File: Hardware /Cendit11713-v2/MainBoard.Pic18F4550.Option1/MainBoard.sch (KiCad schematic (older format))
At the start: 54 parts, among them J1 RESET_CON

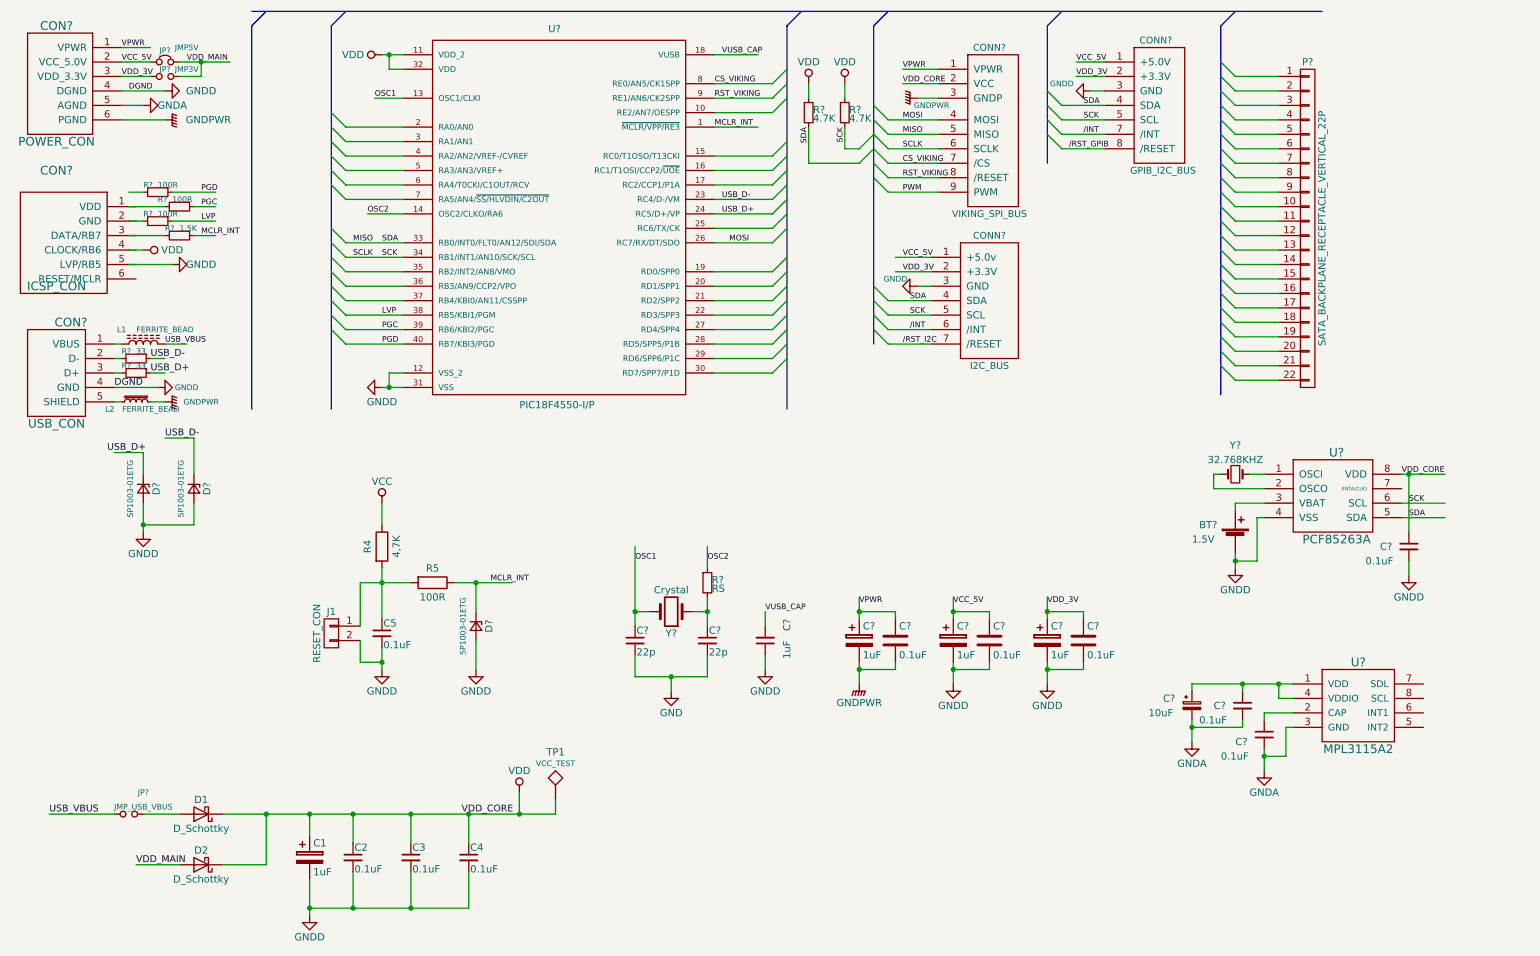
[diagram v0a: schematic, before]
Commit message: Trabajo en Cendit11713 + CenditLab.Reducido
  - En CenditLab revision de codigo
  - En Cendit11713 diseño de tarjeta madre, se crean dos opciones
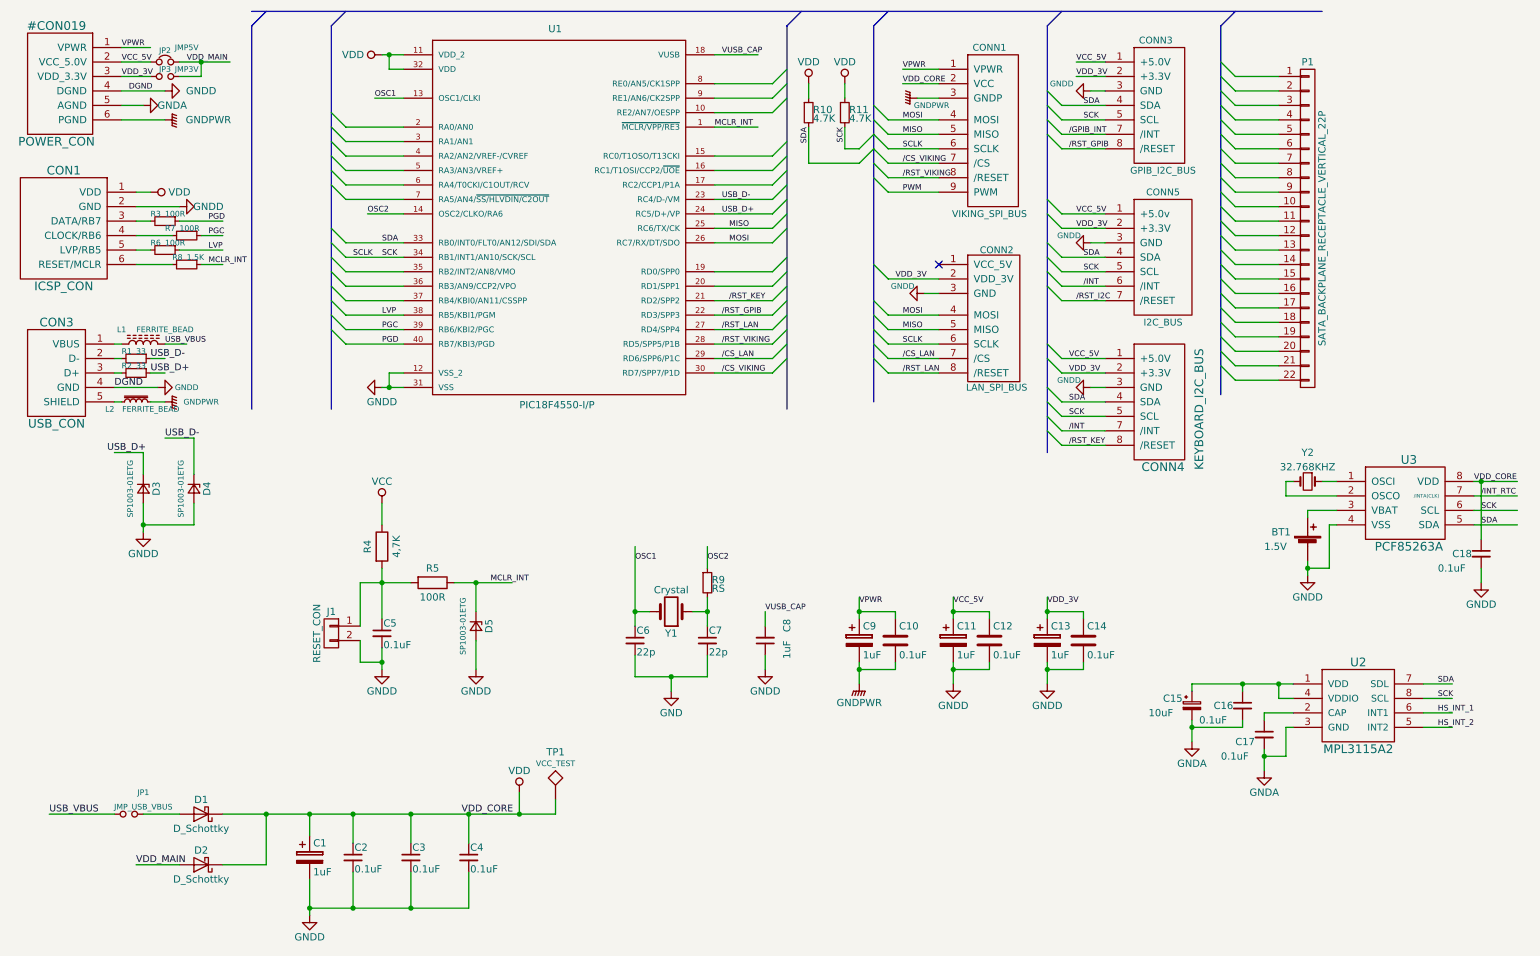
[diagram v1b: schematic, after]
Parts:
- removed CON?: ICSP_CON, symbol ICSP_CON
- removed CON?: POWER_CON, symbol POWER_CON
- added CON1: ICSP_CON, Pin_Headers:Pin_Header_Straight_2x03_Pitch2.54mm, symbol ICSP_CON
- added CONN2: LAN_SPI_BUS, CenditFootprints:SATA_RECEPTACLE_VERTICAL_SMT_6P_7P, symbol LAN_SPI_BUS
- added CONN4: KEYBOARD_I2C_BUS, CenditFootprints:SATA_RECEPTACLE_VERTICAL_SMT_6P_7P, symbol KEYBOARD_I2C_BUS
- C1: footprint (none) -> Capacitors_SMD:C_1206_HandSoldering
- C10, C12, C14, C16, C17, C18: renamed from C?; footprint (none) -> Capacitors_SMD:C_0805_HandSoldering
- C11, C13, C15, C8, C9: renamed from C?; footprint (none) -> Capacitors_SMD:C_1206_HandSoldering
- C2, C3, C4, C5: footprint (none) -> Capacitors_SMD:C_0805_HandSoldering
- C6, C7: renamed from C?; footprint (none) -> Capacitors_SMD:C_0603_HandSoldering
- CON3: renamed from CON?; footprint (none) -> CenditFootprints:USB_SMT_B
- CONN1, CONN3: renamed from CONN?; footprint (none) -> CenditFootprints:SATA_RECEPTACLE_VERTICAL_SMT_6P_7P
- D1, D2: footprint (none) -> CenditFootprints:SP1003-01ETG
- D3, D4, D5: renamed from D?; footprint (none) -> CenditFootprints:SP1003-01ETG
- J1: footprint (none) -> Pin_Headers:Pin_Header_Straight_1x02_Pitch2.54mm
- JP1, JP2, JP3: renamed from JP?; footprint (none) -> Pin_Headers:Pin_Header_Straight_1x02_Pitch2.54mm
- L1, L2: footprint (none) -> Choke_Axial_ThroughHole:Choke_Horizontal_RM10mm
- P1: renamed from P?; footprint (none) -> CenditFootprints:SATA_BACKPLANE_RECEPTACLE_VERTICAL_22P
- R1, R2: renamed from R?; footprint (none) -> Resistors_SMD:R_0603_HandSoldering
- R10, R11, R3, R6, R7, R8, R9: renamed from R?; footprint (none) -> Resistors_SMD:R_0805_HandSoldering
- R4, R5: footprint (none) -> Resistors_SMD:R_0805_HandSoldering
- U1: renamed from U?; footprint DIP254P1524X635-40 -> PIC18F4550-I_P:DIP254P1524X635-40
- U2: renamed from U?; footprint (none) -> CenditFootprints:MPL3115A2
- U3: renamed from U?; footprint (none) -> CenditFootprints:PCF85263A_SO8
- Y1: renamed from Y?; footprint (none) -> Crystals:Crystal_HC49-4H_Vertical
- Y2: renamed from Y?; footprint (none) -> Crystals:Crystal_C26-LF_d2.1mm_l6.5mm_Vertical
- gave numbers to parts that had none: 2
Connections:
- net labels added: /CS_LAN, /CS_VIKING, /GPIB_INT, /INT_RTC, /RST_KEY, /RST_LAN, /RST_VIKING, HS_INT_1, HS_INT_2, POWER_CON
- net labels removed: CS_VIKING, RST_VIKING
- wire segments 213 -> 232
- no-connect marks 0 -> 1
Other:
- moved on the sheet: BT1, C18, CONN5, R3, R6, R7, R8, U3, Y2

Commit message: Respaldo rapido
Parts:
- CON1: symbol ICSP_CON -> ICSP_CON-RESCUE-MainBoard
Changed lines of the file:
@@
 	1550 1200 1400 1200
 $Comp
-L POWER_CON #CON019
+L POWER_CON-RESCUE-MainBoard #CON019
 U 1 1 5A03F0DE
 P 750 1550
-F 0 "#CON019" H 550 2450 60  0000 C CNN
+F 0 "#CON019" H 550 2450 60  0001 C CNN
 F 1 "POWER_CON" H 550 1650 60  0000 C CNN
 F 2 "" H 750 1550 60  0001 C CNN
@@
 $EndComp
 $Comp
-L ICSP_CON CON1
+L ICSP_CON-RESCUE-MainBoard CON1
 U 1 1 5A0565BC
 P 700 2400
